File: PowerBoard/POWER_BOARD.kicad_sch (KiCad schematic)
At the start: 35 parts, among them J3 Molex Microfit 2.0, Q2 IRL520NSTRLPBF, Q3 FGH75T65SQD-F155, T1 DA2034, U1 SC09147, U2 LT3750, U4 MCP14A0454-E/SN

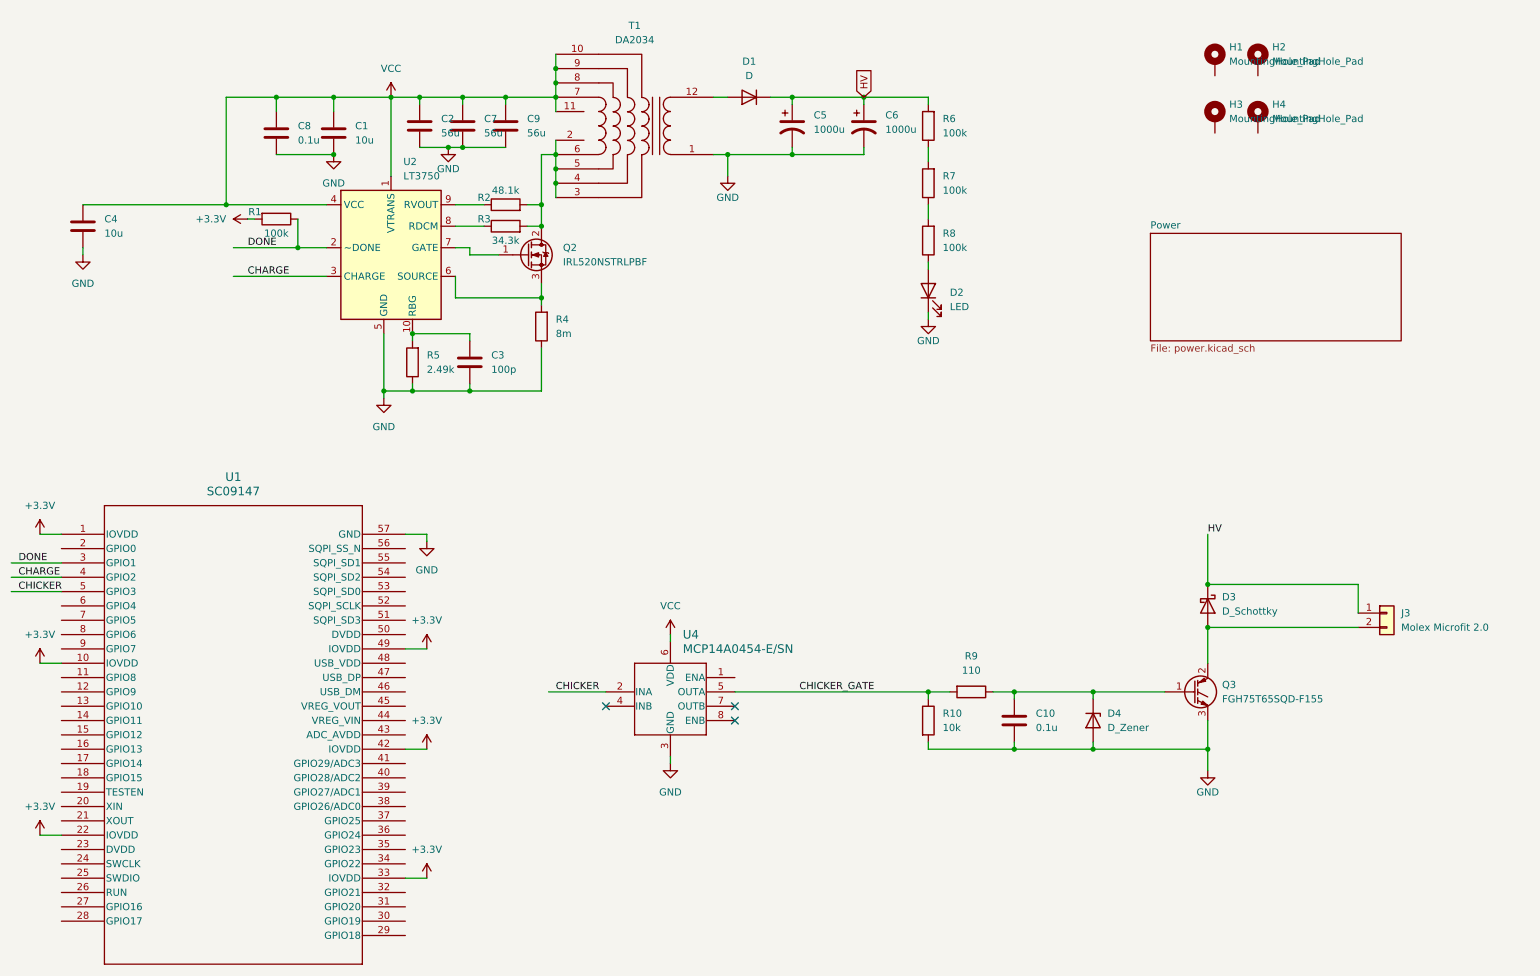
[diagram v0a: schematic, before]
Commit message: added 2040 flashing circuit and battery monitor
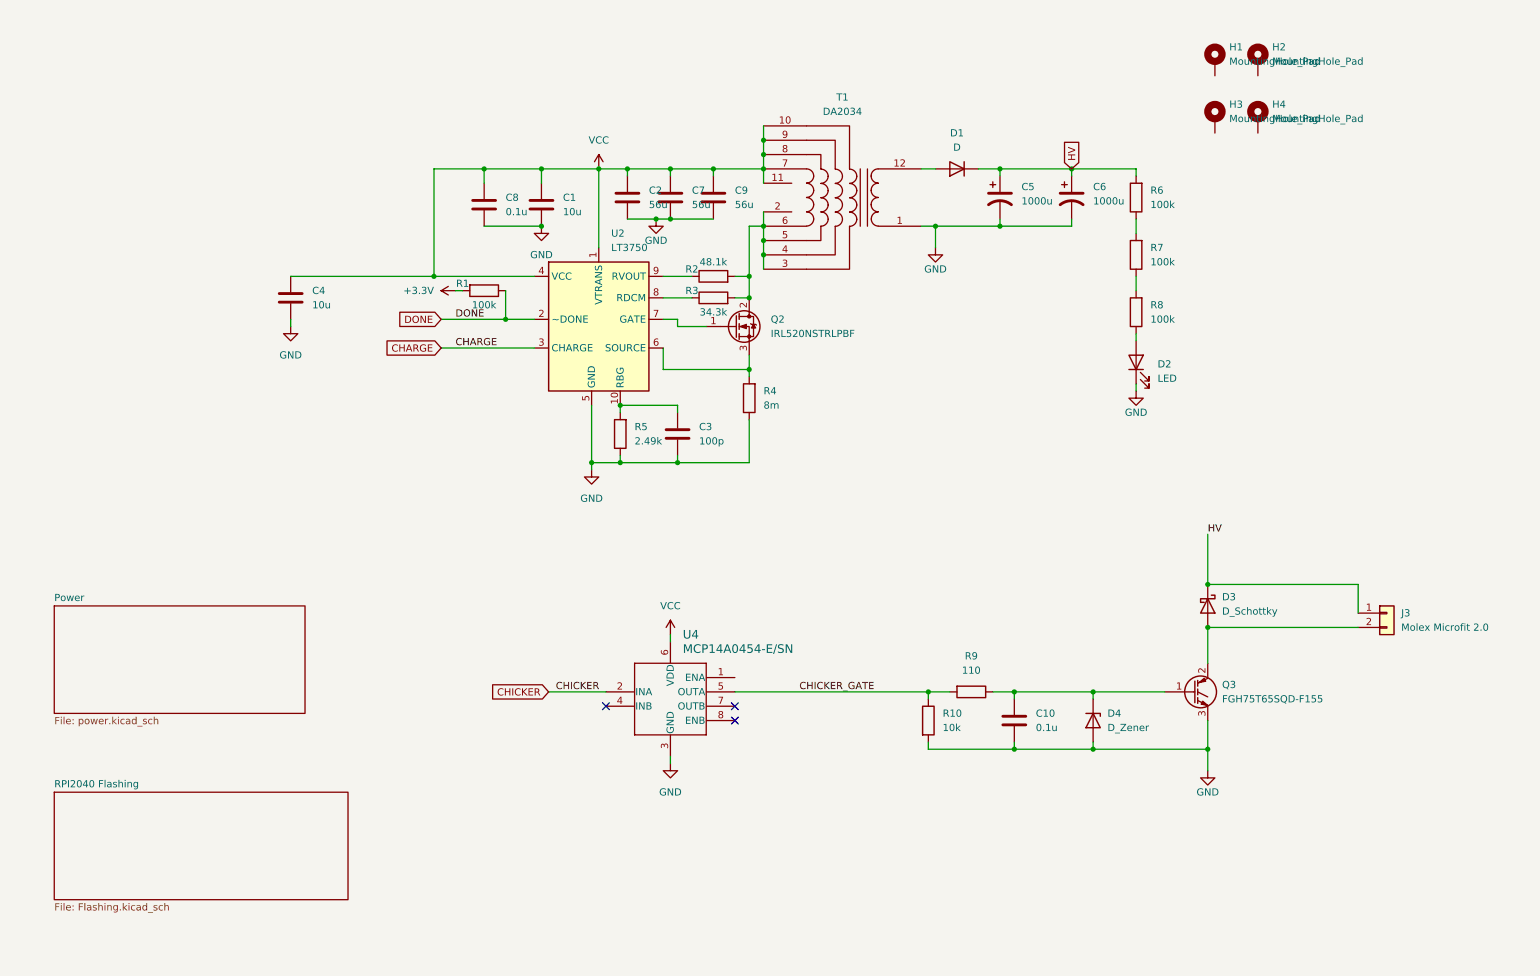
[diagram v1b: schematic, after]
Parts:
- removed U1: SC09147, RPI2040:QFN56_7X7_RPI, symbol bots:SC0914-7
- U2: footprint Package_SO:MSOP-10_3x3mm_P0.5mm -> Package_DFN_QFN:DFN-10-1EP_3x3mm_P0.5mm_EP1.55x2.48mm
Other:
- added sheet RPI2040 Flashing (Flashing.kicad_sch)
- moved on the sheet: C1, C2, C3, C4, C5, C6, C7, C8, C9, D1, D2, Q2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

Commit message: updated board shape + placed most components
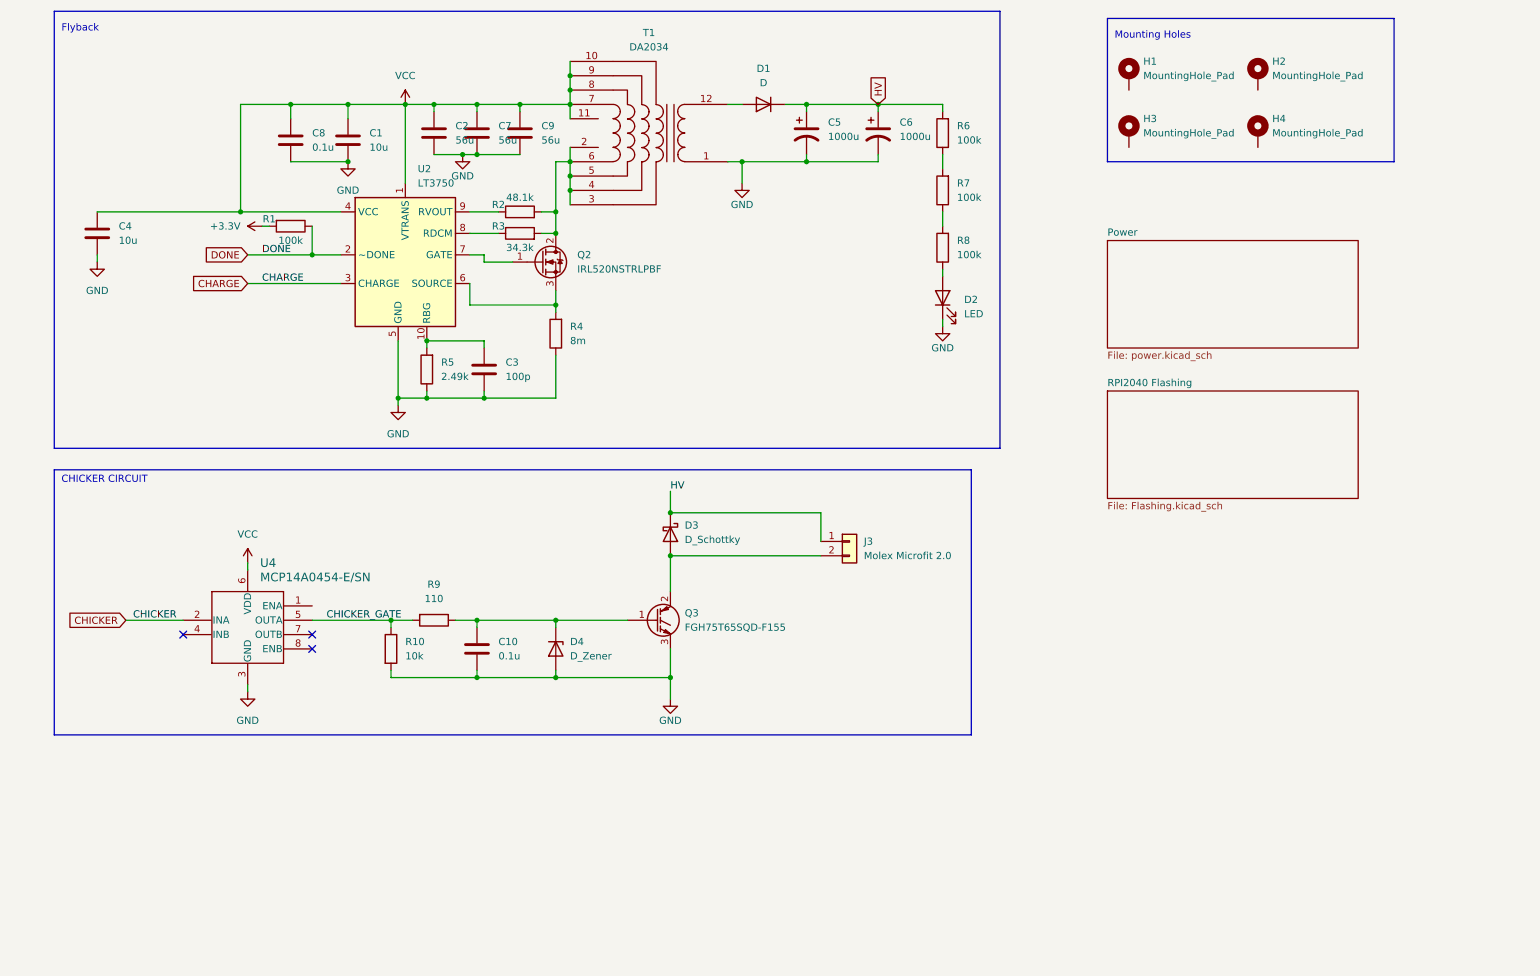
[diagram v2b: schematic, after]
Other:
- note added: "CHICKER CIRCUIT"
- note added: "Flyback"
- note added: "Mounting Holes"
- moved on the sheet: C1, C10, C2, C3, C4, C5, C6, C7, C8, C9, D1, D2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

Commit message: board components mostly placed correctly
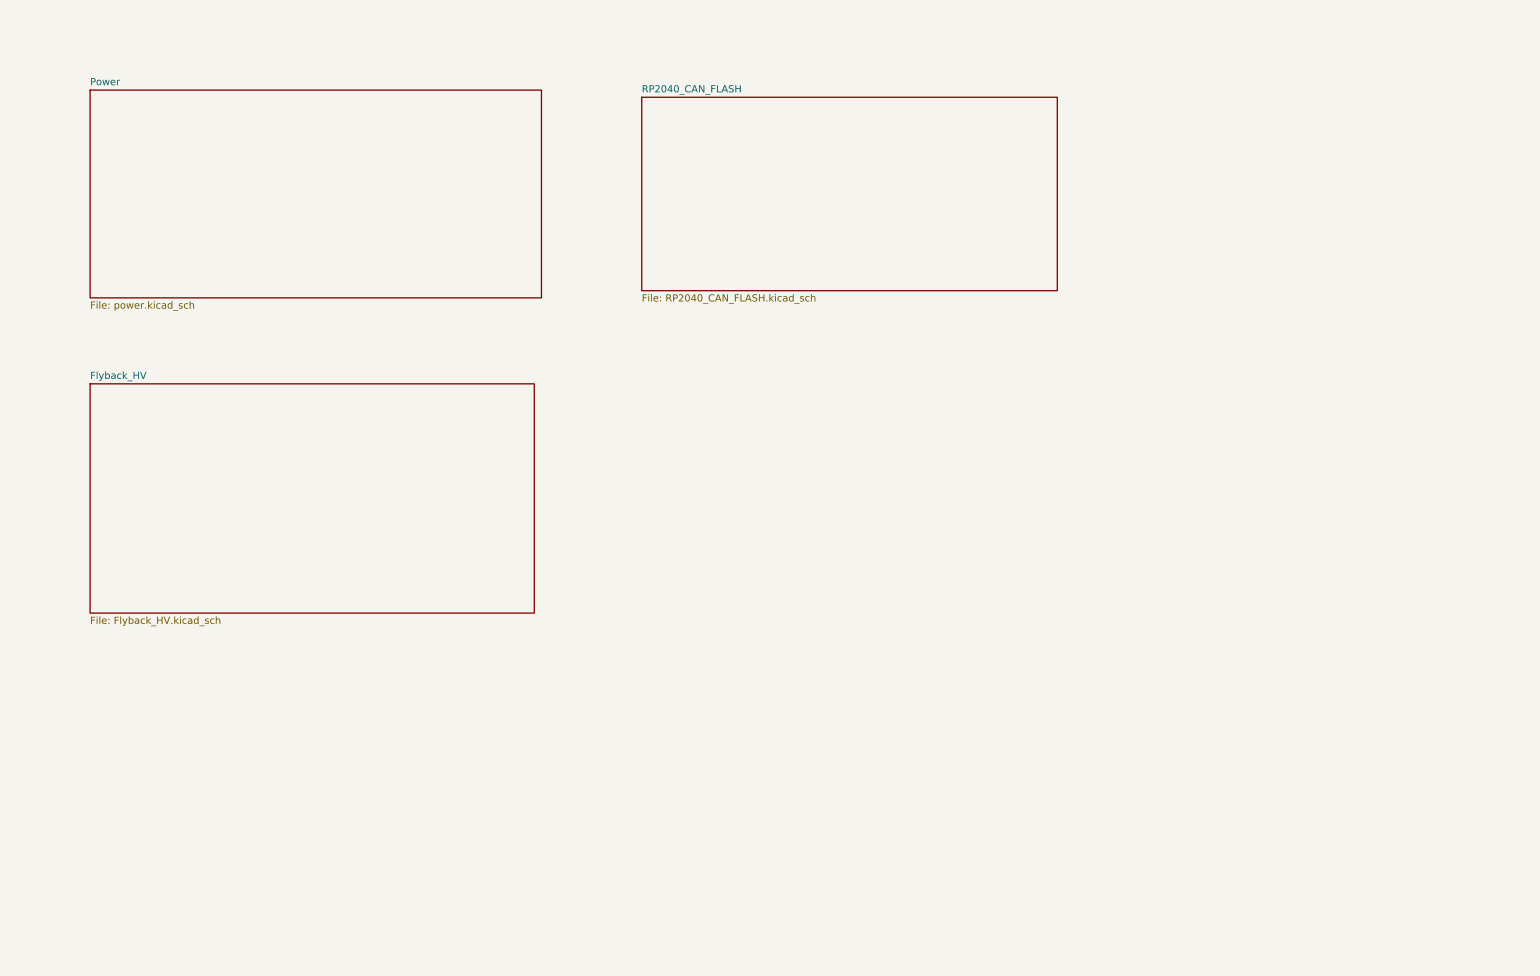
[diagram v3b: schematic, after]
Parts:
- removed C1, C4: 10u, Capacitor_SMD:C_0805_2012Metric, symbol Device:C
- removed C10, C8: 0.1u, Capacitor_SMD:C_0603_1608Metric, symbol Device:C
- removed C2, C7, C9: 56u, Capacitor_SMD:C_0805_2012Metric, symbol Device:C
- removed C3: 100p, Capacitor_SMD:C_0603_1608Metric, symbol Device:C
- removed C5, C6: 1000u, Capacitor_THT:CP_Radial_D25.0mm_P10.00mm_SnapIn, symbol Device:C_Polarized_US
- removed D1: D, Diode_SMD:D_SMB, symbol Device:D
- removed D2: LED, LED_SMD:LED_1206_3216Metric, symbol Device:LED
- removed D3: D_Schottky, Diode_SMD:D_SMC, symbol Device:D_Schottky
- removed D4: D_Zener, Diode_SMD:D_SMA, symbol Device:D_Zener
- removed H1, H2, H3, H4: MountingHole_Pad, MountingHole:MountingHole_2.7mm_M2.5_DIN965_Pad, symbol Mechanical:MountingHole_Pad
- removed J3: Molex Microfit 2.0, Connector_Molex:Molex_KK-396_A-41792-0002_1x02_P3.96mm_Horizontal, symbol Connector_Generic:Conn_01x02
- removed Q2: IRL520NSTRLPBF, Package_TO_SOT_SMD:TO-263-2, symbol Transistor_FET:IRFS4127
- removed Q3: FGH75T65SQD-F155, Package_TO_SOT_THT:TO-247-3_Vertical, symbol Transistor_IGBT:IRG4PF50W
- removed R1, R6, R7, R8: 100k, Resistor_SMD:R_0603_1608Metric, symbol Device:R
- removed R10: 10k, Resistor_SMD:R_0603_1608Metric, symbol Device:R
- removed R2: 48.1k, Resistor_SMD:R_0603_1608Metric, symbol Device:R
- removed R3: 34.3k, Resistor_SMD:R_0603_1608Metric, symbol Device:R
- removed R4: 8m, Resistor_SMD:R_1206_3216Metric, symbol Device:R
- removed R5: 2.49k, Resistor_SMD:R_0603_1608Metric, symbol Device:R
- removed R9: 110, Resistor_SMD:R_0603_1608Metric, symbol Device:R
- removed T1: DA2034, DA2034:SOIC12_DA2034-ALD_COC, symbol bots:DA2034
- removed U2: LT3750, Package_DFN_QFN:DFN-10-1EP_3x3mm_P0.5mm_EP1.55x2.48mm, symbol bots:LT3750
- removed U4: MCP14A0454-E/SN, SOIC8_SN_MCH, symbol bots:MCP14A0454-E_SN
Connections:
- no-connect marks 3 -> 0
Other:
- sheet RPI2040 Flashing renamed RP2040_CAN_FLASH
- added sheet Flyback_HV (Flyback_HV.kicad_sch)
- sheet RP2040_CAN_FLASH: file Flashing.kicad_sch -> RP2040_CAN_FLASH.kicad_sch
- note removed: "CHICKER CIRCUIT"
- note removed: "Flyback"
- note removed: "Mounting Holes"
